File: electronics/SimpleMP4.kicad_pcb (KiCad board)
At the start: 2 copper layers, 119 parts, among them J1 USB_OTG, Q1 8050, Q2 SI2305, Q3 SI2305, Q4 8050, Q5 8550, Q6 SI2305, Q7 8550, U1 OCP8020, U2 RK2608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

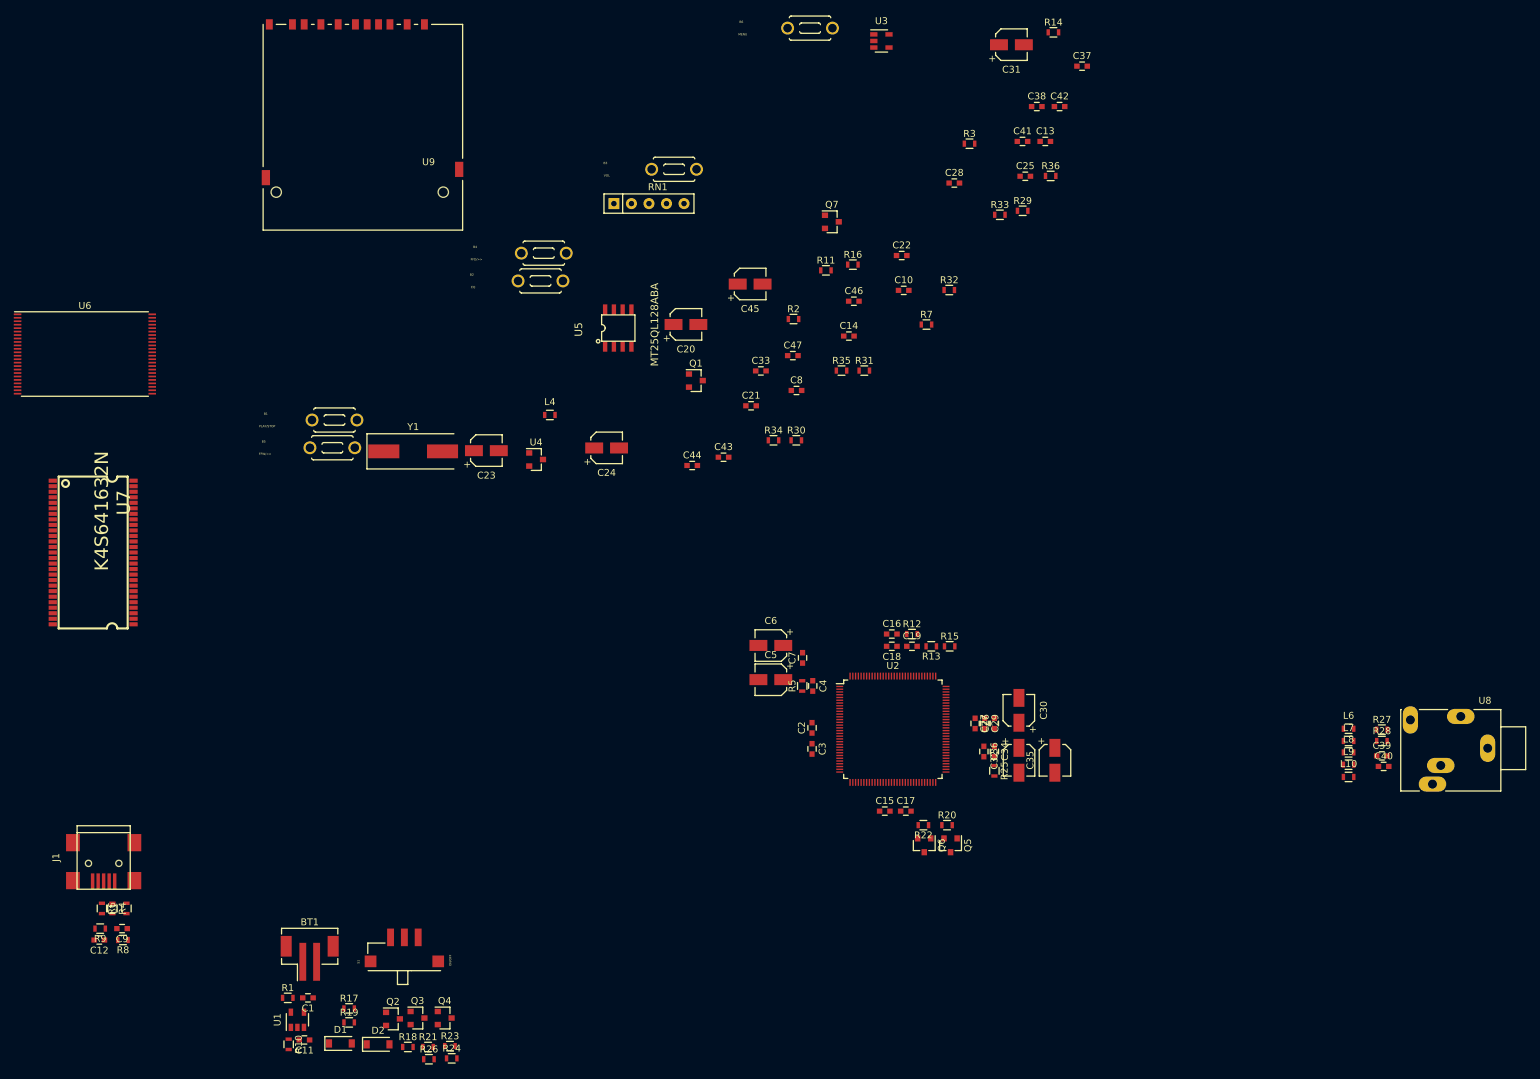
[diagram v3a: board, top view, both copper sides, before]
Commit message: placed more components and defined board edge
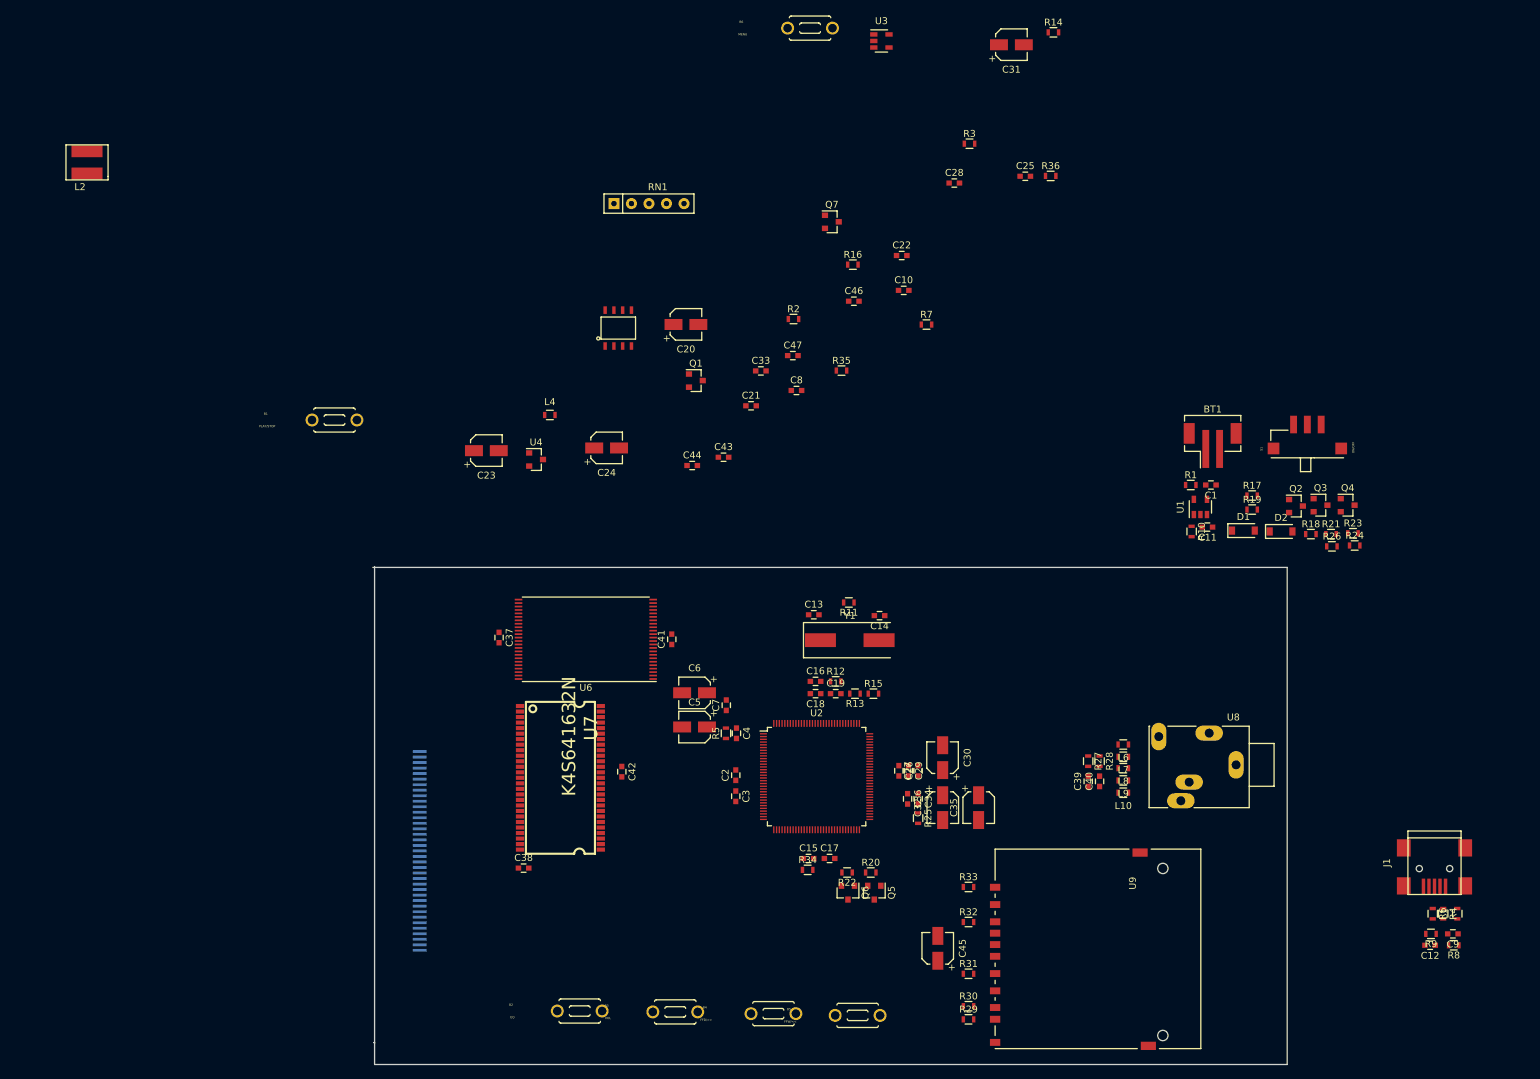
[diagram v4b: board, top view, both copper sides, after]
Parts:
- added J2: DISPLAY, footprints:KD024B, B.Cu at (105.3, 145.7)
- added L2: 4.7uH, footprints:CR43NP-4R7MC, F.Cu at (57.1, 46.4)
- U5: footprint SOP-8:SOP-8 -> footprints:SOP-8
- moved C12 192.8 mm to (251.7, 159.8)
- moved C9 192.8 mm to (255.0, 158.1)
- moved J1 192.8 mm to (252.3, 148.5)
- moved L1 192.8 mm to (255.7, 155.2)
- moved R4 192.8 mm to (253.6, 155.2)
- moved R6 192.8 mm to (252.1, 155.2)
- moved R8 192.8 mm to (255.1, 159.8)
- moved R9 192.8 mm to (251.8, 158.1)
- moved U9 160.0 mm to (200.9, 160.3), turned to 90 degrees
- moved BT1 150.4 mm to (220.2, 86.7)
- moved C1 150.4 mm to (220.0, 93.1)
- moved C11 150.4 mm to (219.5, 99.2)
- moved D1 150.4 mm to (224.7, 99.7)
- moved Q2 150.4 mm to (232.3, 96.1)
- moved R1 150.4 mm to (217.0, 93.1)
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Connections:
- R18 pad 2: Net-(R18-Pad2) -> GND
- R23 pad 1: Net-(R18-Pad2) -> GND
- R26 pad 1: Net-(R18-Pad2) -> GND
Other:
- board outline added: 132.5 x 72.1 mm

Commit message: pausing for now
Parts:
- moved B1 188.2 mm to (275.0, 131.8), turned to 180 degrees
- moved B5 111.9 mm to (275.3, 135.6)
- moved B2 111.9 mm to (235.1, 135.0)
- moved B3 111.9 mm to (248.9, 135.1)
- moved B4 111.9 mm to (263.1, 135.4)
- moved L2 85.0 mm to (135.1, 80.1)
- moved J1 78.1 mm to (183.6, 111.3)
- moved U9 77.6 mm to (132.3, 196.8), turned to 270 degrees
- moved R9 77.5 mm to (183.1, 122.2)
- moved C9 77.5 mm to (186.3, 122.2)
- moved L1 77.5 mm to (186.9, 119.3)
- moved C12 77.5 mm to (183.0, 123.8)
- moved R4 77.5 mm to (184.9, 119.3)
- moved R6 77.5 mm to (183.4, 119.3)
- moved R8 77.5 mm to (186.4, 123.8)
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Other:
- board size 132.5 x 72.1 mm -> 124.7 x 72.1 mm

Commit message: added inductor footprints and starting to route
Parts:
- added L3: 10uH, Inductors_SMD:L_1210, F.Cu at (187.3, 137.0)
- added L5: 10uH, Inductors_SMD:L_1210, F.Cu at (187.3, 140.6)
- moved U9 168.8 mm to (248.0, 73.9), turned to 90 degrees
- moved R33 163.9 mm to (232.0, 64.9), turned to 0 degrees
- moved R32 155.3 mm to (232.0, 70.0), turned to 0 degrees
- moved C45 144.1 mm to (227.6, 73.8), turned to 90 degrees
- moved R31 142.9 mm to (232.0, 77.5), turned to 0 degrees
- moved R30 135.4 mm to (232.0, 82.2), turned to 0 degrees
- moved R29 132.4 mm to (232.0, 84.1), turned to 0 degrees
- moved C42 85.2 mm to (50.5, 148.3)
- moved U7 85.2 mm to (41.7, 149.2)
- moved C38 85.2 mm to (36.3, 162.3)
- moved J2 81.6 mm to (100.3, 59.8)
- moved C41 80.2 mm to (55.5, 128.7)
- moved C37 80.2 mm to (30.0, 128.5)
- moved U6 80.2 mm to (42.5, 128.8)
- moved R11 31.8 mm to (181.1, 79.9)
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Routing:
- net /VB: track 0.00 -> 11.1 mm
- net Net-(Q2-Pad3): track 0.00 -> 2.00 mm
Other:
- board size 124.7 x 72.1 mm -> 124.6 x 72.1 mm
- net class Default: clearance 0.2 -> 0.1524; trace_width 0.25 -> 0.1524; via_dia 0.6 -> 0.6858; via_drill 0.4 -> 0.3302
- rule trace_clearance: 0.2 -> 0.1524
- rule trace_min: 0.2 -> 0.1524
- rule via_min_drill: 0.3 -> 0.3302
- rule via_min_size: 0.4 -> 0.6858

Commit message: that's it for today
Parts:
- moved C31 125.0 mm to (164.5, 151.4), turned to 90 degrees
- moved U9 122.9 mm to (181.4, 177.2)
- moved R29 122.5 mm to (165.9, 187.1)
- moved R30 122.5 mm to (165.9, 185.2)
- moved R33 122.5 mm to (165.9, 168.0)
- moved C45 122.5 mm to (161.4, 176.8)
- moved R31 122.5 mm to (165.9, 180.5)
- moved R32 122.5 mm to (165.9, 173.0)
- moved R14 119.2 mm to (175.3, 144.7)
- moved U3 117.0 mm to (171.2, 145.7)
- moved R3 114.1 mm to (110.3, 129.9), turned to 90 degrees
- moved C28 106.0 mm to (179.3, 155.3)
- moved C25 99.0 mm to (165.6, 143.5), turned to 180 degrees
- moved R7 88.9 mm to (116.4, 133.2), turned to 180 degrees
- moved C10 87.6 mm to (117.0, 130.2), turned to 270 degrees
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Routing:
- net /VB: track 11.1 -> 0.00 mm
- net Net-(Q2-Pad3): track 2.00 -> 0.00 mm
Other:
- board size 124.6 x 72.1 mm -> 126.5 x 74.2 mm

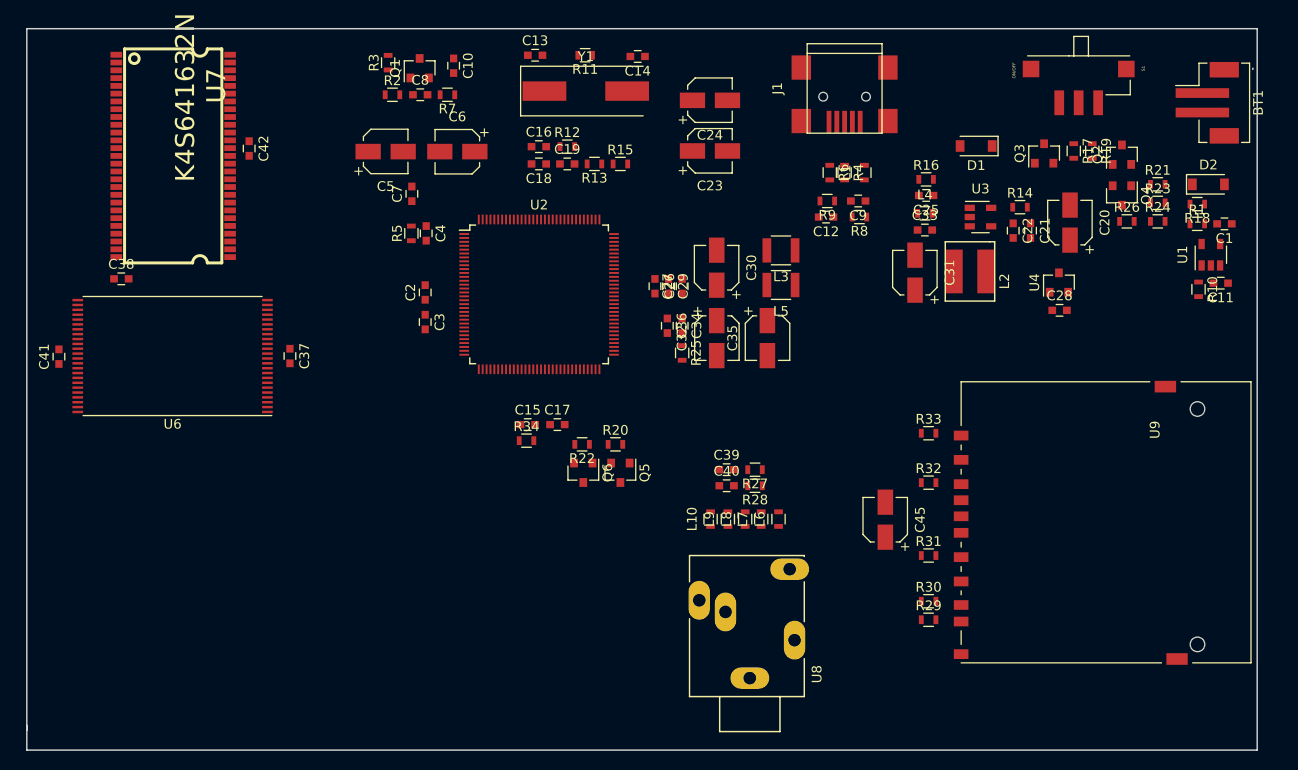
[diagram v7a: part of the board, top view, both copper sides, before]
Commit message: added partial routing
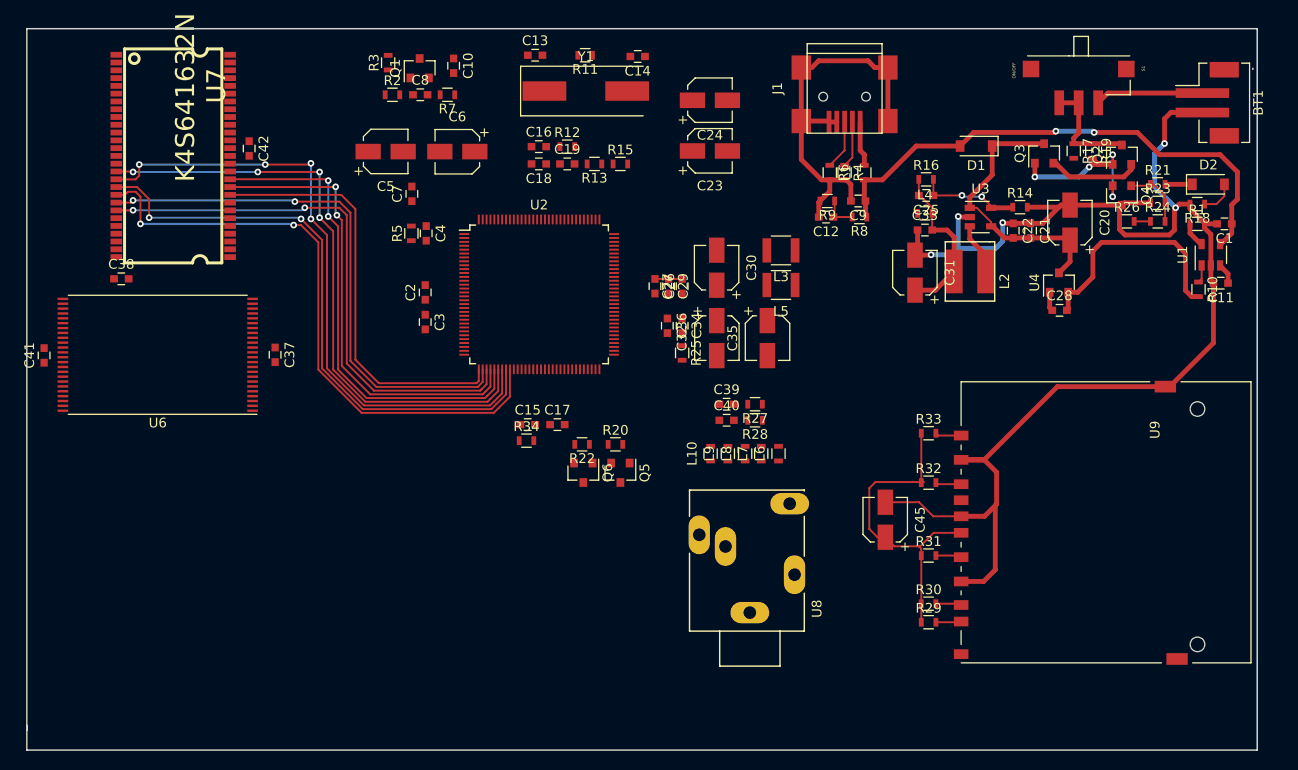
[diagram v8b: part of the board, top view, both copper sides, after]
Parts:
- moved C39 6.73 mm to (145.1, 165.0)
- moved C40 6.73 mm to (145.1, 166.6)
- moved L10 6.73 mm to (143.4, 170.1)
- moved L6 6.73 mm to (150.4, 170.1)
- moved L7 6.73 mm to (148.7, 170.1)
- moved L8 6.73 mm to (147.0, 170.1)
- moved L9 6.73 mm to (145.2, 170.1)
- moved R27 6.73 mm to (148.0, 165.0)
- moved R28 6.73 mm to (148.0, 166.6)
- moved U8 6.73 mm to (152.1, 182.5)
- moved C37 1.53 mm to (98.7, 159.9)
- moved U6 1.53 mm to (86.6, 159.9)
- moved C41 1.53 mm to (74.9, 160.0)
- moved R29 0.25 mm to (165.9, 187.4)
- moved R30 0.25 mm to (165.9, 185.5)
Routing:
- net GND: track 0.00 -> 189.1 mm, vias 0 -> 5
- net /CASN: track 0.00 -> 65.7 mm, vias 0 -> 4
- net /WEN: track 0.00 -> 62.9 mm, vias 0 -> 4
- net /CSN: track 0.00 -> 62.8 mm, vias 0 -> 2
- net /RASN: track 0.00 -> 61.8 mm, vias 0 -> 2
- net VCC: track 0.00 -> 57.6 mm
- net /BA1: track 0.00 -> 56.7 mm, vias 0 -> 2
- net /BA0: track 0.00 -> 56.1 mm, vias 0 -> 2
- net +5V: track 0.00 -> 54.3 mm, vias 0 -> 2
- net /CLK: track 0.00 -> 49.7 mm, vias 0 -> 2
- net /CKE: track 0.00 -> 48.1 mm, vias 0 -> 2
- net /A12: track 0.00 -> 44.0 mm
- net /BATT: track 0.00 -> 28.5 mm
- net Net-(Q2-Pad1): track 0.00 -> 17.4 mm, vias 0 -> 4
- net /VDDO: track 0.00 -> 16.8 mm
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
